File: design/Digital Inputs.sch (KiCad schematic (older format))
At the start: 16 parts

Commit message: decide to put CPU on mainboard, drop core board design
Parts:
- removed D?: LED, symbol LED
- removed JP?: JUMPER, symbol JUMPER
- removed R?: 2K4, symbol R
- removed R?: 1K, symbol R
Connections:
- net labels removed: +5V_MICRO, GND, PA6
- wire segments 31 -> 23
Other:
- note added: "????????????\n\nspeed sensor input 6v square wave, need resistors"
- note removed: "Enable Serial Monitor"
- moved on the sheet: D?, Q?, R?

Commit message: revise schema to be full pin compatible with stock ECU
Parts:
- removed D?: LED, symbol LED
- removed Q?: MMBT3904LT1, symbol NPN
- removed R?: 330-1/4W, symbol R
- removed R?: 1K, symbol R
- removed R?: 1K-1/4W, symbol R
- removed R?: 2K4-1/4W, symbol R
- added D22, D25: ZENER, symbol ZENER
- added D26: 5.6V, symbol ZENER
- added R57, R62: R, symbol R
- added R60: 1K, symbol R
- added R61: 470R, symbol R
- gave numbers to parts that had none: 6
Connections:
- net labels added: GND
- net labels removed: +12V_SWITCHED, HCURGND, SENSORGND
- wire segments 23 -> 24
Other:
- note removed: "????????????\n\nspeed sensor input 6v square wave, need resistors"
- moved on the sheet: D21, D23, D24, R56, R58, R59

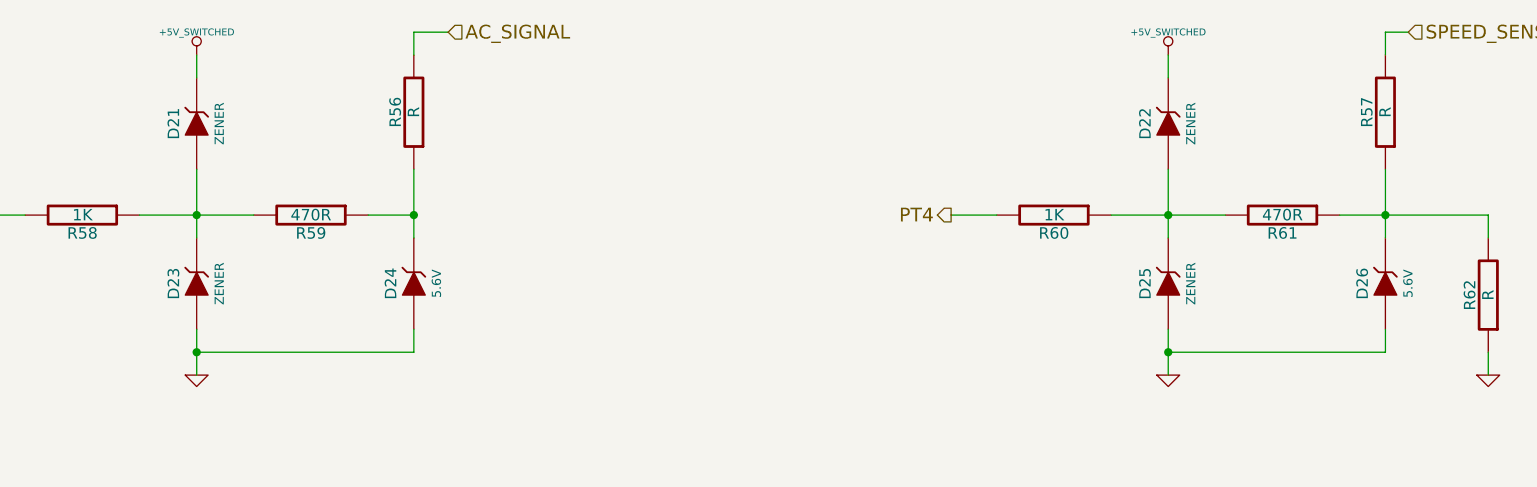
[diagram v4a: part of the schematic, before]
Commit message: add missing diodes, re-generate netlist, assign all footprints, ready to layout
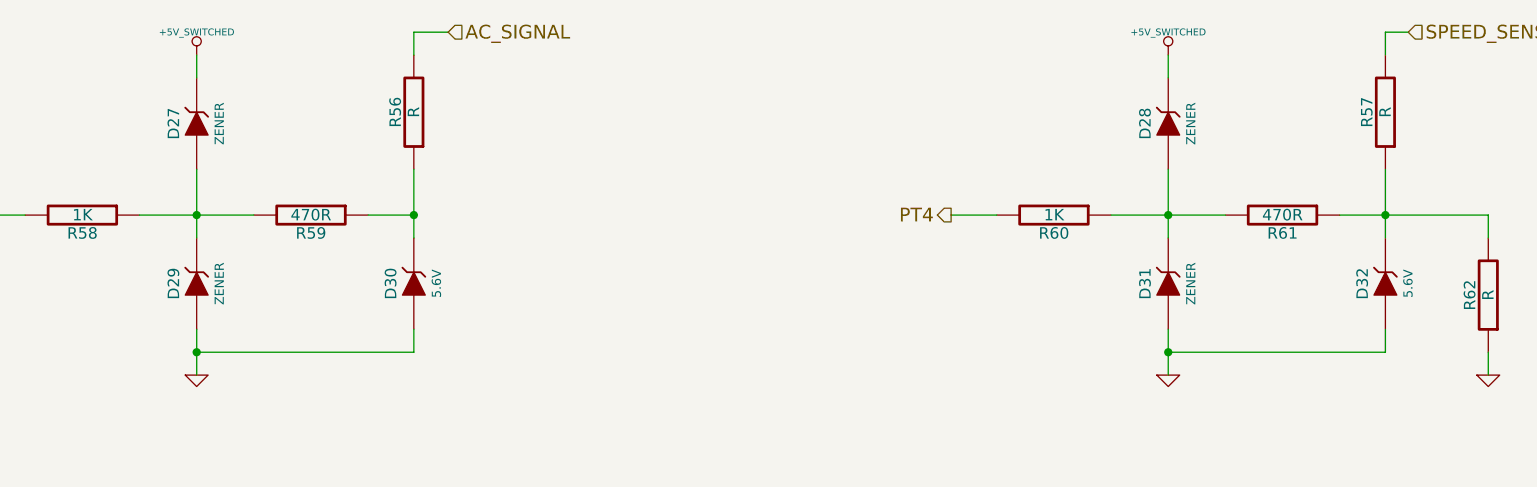
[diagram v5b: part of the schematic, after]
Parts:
- renumbered D21 to D27, D22 to D28, D23 to D29, D24 to D30, D25 to D31, D26 to D32
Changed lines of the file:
@@
-EESchema Schematic File Version 2  date 03/01/2012 09:04:48
+EESchema Schematic File Version 2  date 12/01/2012 20:05:35
 LIBS:power
 LIBS:device
@@
 $Descr A4 11700 8267
 Sheet 9 12
-Title ""
-Date "3 jan 2012"
-Rev ""
-Comp ""
+Title "Digital Inputs"
+Date "12 jan 2012"
+Rev "0.01"
+Comp "diyefi.org"
 Comment1 ""
 Comment2 ""
@@
 $EndComp
 $Comp
-L ZENER D22
+L ZENER D28
 U 1 1 4F01437A
 P 7300 3050
-F 0 "D22" H 7300 3150 50  0000 C CNN
+F 0 "D28" H 7300 3150 50  0000 C CNN
 F 1 "ZENER" H 7300 2950 40  0000 C CNN
 	1    7300 3050
@@
 $EndComp
 $Comp
-L ZENER D25
+L ZENER D31
 U 1 1 4F014379
 P 7300 3750
-F 0 "D25" H 7300 3850 50  0000 C CNN
+F 0 "D31" H 7300 3850 50  0000 C CNN
 F 1 "ZENER" H 7300 3650 40  0000 C CNN
 	1    7300 3750
@@
 $EndComp
 $Comp
-L ZENER D26
+L ZENER D32
 U 1 1 4F014377
 P 8250 3750
-F 0 "D26" H 8250 3850 50  0000 C CNN
+F 0 "D32" H 8250 3850 50  0000 C CNN
 F 1 "5.6V" H 8250 3650 40  0000 C CNN
 	1    8250 3750
@@
 $EndComp
 $Comp
-L ZENER D24
+L ZENER D30
 U 1 1 4E94175B
 P 4000 3750
-F 0 "D24" H 4000 3850 50  0000 C CNN
+F 0 "D30" H 4000 3850 50  0000 C CNN
 F 1 "5.6V" H 4000 3650 40  0000 C CNN
 	1    4000 3750
@@
 $EndComp
 $Comp
-L ZENER D23
+L ZENER D29
 U 1 1 4E941736
 P 3050 3750
-F 0 "D23" H 3050 3850 50  0000 C CNN
+F 0 "D29" H 3050 3850 50  0000 C CNN
 F 1 "ZENER" H 3050 3650 40  0000 C CNN
 	1    3050 3750
@@
 $EndComp
 $Comp
-L ZENER D21
+L ZENER D27
 U 1 1 4E941735
 P 3050 3050
-F 0 "D21" H 3050 3150 50  0000 C CNN
+F 0 "D27" H 3050 3150 50  0000 C CNN
 F 1 "ZENER" H 3050 2950 40  0000 C CNN
 	1    3050 3050

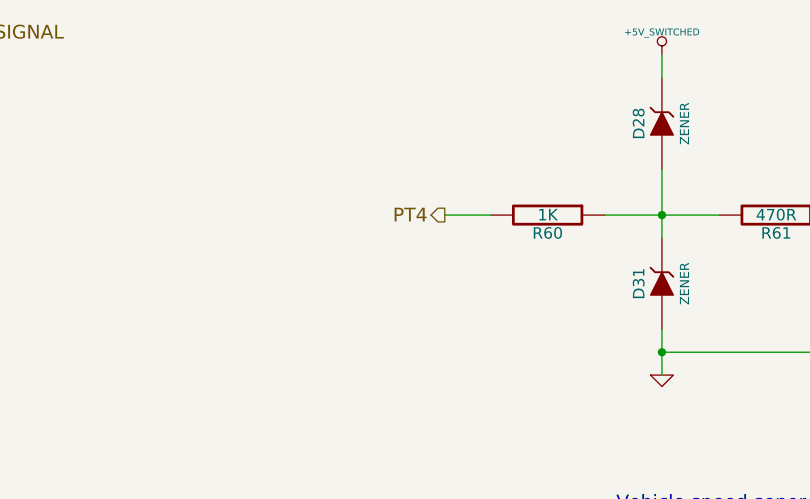
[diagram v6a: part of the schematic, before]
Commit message: use max9924 to replace ncv1124, add narrow band oxygen sensor differential input circuit, put all component into PCB edge
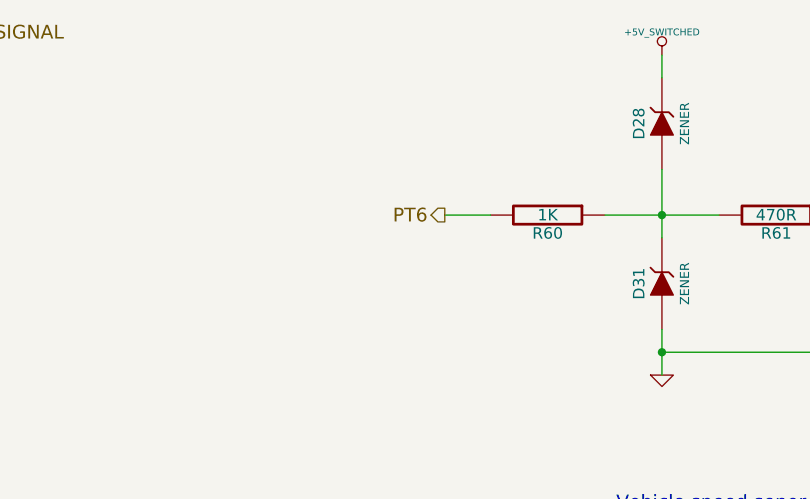
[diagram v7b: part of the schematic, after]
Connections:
- net PT4 renamed PT6
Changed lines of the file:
@@
-EESchema Schematic File Version 2  date 14/01/2012 13:46:11
+EESchema Schematic File Version 2  date 21/01/2012 01:12:26
 LIBS:power
 LIBS:device
@@
 LIBS:contrib
 LIBS:valves
+LIBS:freeEMS_lib
 LIBS:mainboard-cache
 EELAYER 25  0
 EELAYER END
 $Descr A4 11700 8267
-Sheet 9 12
+Sheet 2 12
 Title "Digital Inputs"
-Date "14 jan 2012"
+Date "20 jan 2012"
 Rev "0.01"
 Comp "diyefi.org"
@@
 	8700 3450 8700 3550
 $Comp
-L GND #PWR98
+L GND #PWR5
 U 1 1 4F014611
 P 8700 4150
-F 0 "#PWR98" H 8700 4150 30  0001 C CNN
+F 0 "#PWR5" H 8700 4150 30  0001 C CNN
 F 1 "GND" H 8700 4080 30  0001 C CNN
 	1    8700 4150
@@
 $EndComp
 $Comp
-L +5V_SWITCHED #PWR95
+L +5V_SWITCHED #PWR2
 U 1 1 4F01437B
 P 7300 2750
-F 0 "#PWR95" H 7300 2700 20  0001 C CNN
+F 0 "#PWR2" H 7300 2700 20  0001 C CNN
 F 1 "+5V_SWITCHED" H 7300 2850 30  0000 C CNN
 	1    7300 2750
@@
 Vehicle speed senor input
 $Comp
-L GND #PWR97
+L GND #PWR4
 U 1 1 4F014374
 P 7300 4150
-F 0 "#PWR97" H 7300 4150 30  0001 C CNN
+F 0 "#PWR4" H 7300 4150 30  0001 C CNN
 F 1 "GND" H 7300 4080 30  0001 C CNN
 	1    7300 4150
@@
 $EndComp
 Text HLabel 6350 3450 0    60   Output ~ 0
-PT4
-$Comp
-L GND #PWR96
+PT6
+$Comp
+L GND #PWR3
 U 1 1 4F008CAA
 P 3050 4150
-F 0 "#PWR96" H 3050 4150 30  0001 C CNN
+F 0 "#PWR3" H 3050 4150 30  0001 C CNN
 F 1 "GND" H 3050 4080 30  0001 C CNN
 	1    3050 4150
@@
 $EndComp
 $Comp
-L +5V_SWITCHED #PWR94
+L +5V_SWITCHED #PWR1
 U 1 1 4E941734
 P 3050 2750
-F 0 "#PWR94" H 3050 2700 20  0001 C CNN
+F 0 "#PWR1" H 3050 2700 20  0001 C CNN
 F 1 "+5V_SWITCHED" H 3050 2850 30  0000 C CNN
 	1    3050 2750
